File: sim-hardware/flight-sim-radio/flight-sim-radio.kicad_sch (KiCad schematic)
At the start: 0 parts

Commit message: Started on schematic
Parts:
- added U1, U2, U3: LTC-4627JR, Display_7Segment:LTC-4627Jx, symbol Display_Character:LTC-4627JR
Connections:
- new net GND: U1.4 (CAL), U2.4 (CAL), U3.4 (CAL)
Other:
- note added: "Seven Segment Displays"

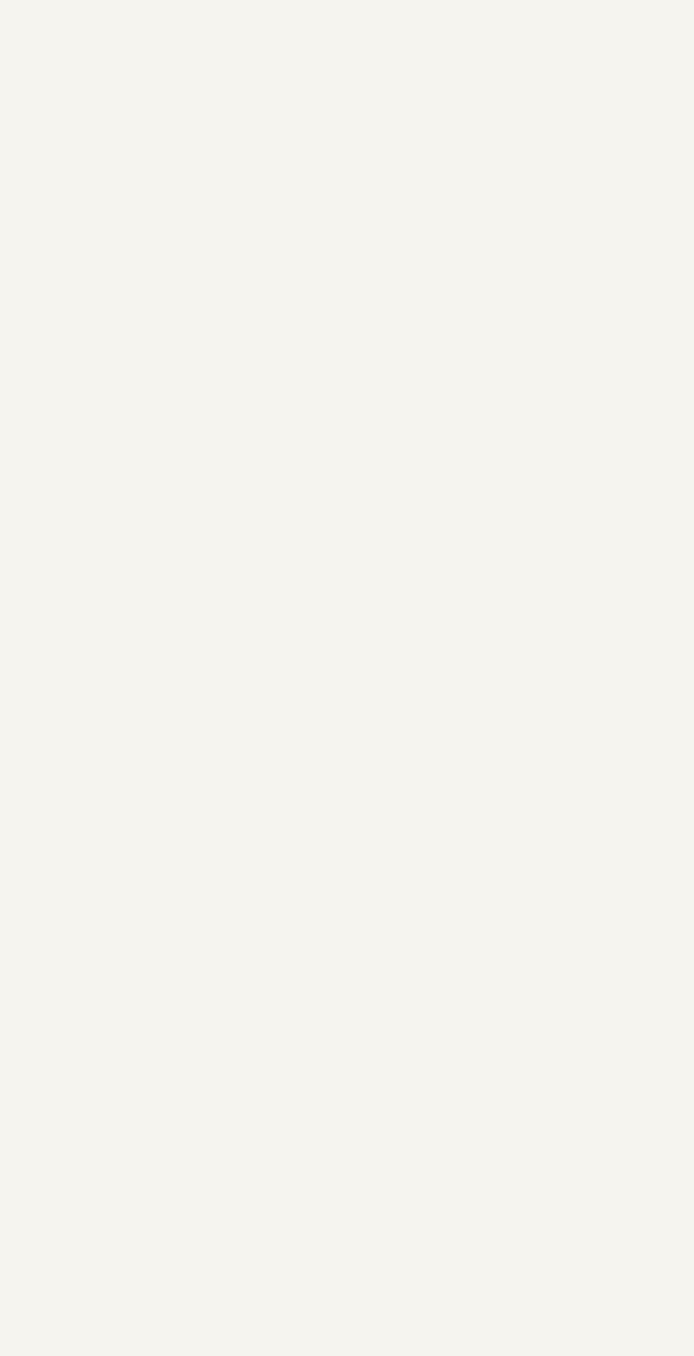
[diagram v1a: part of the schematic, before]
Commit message: LED driver added
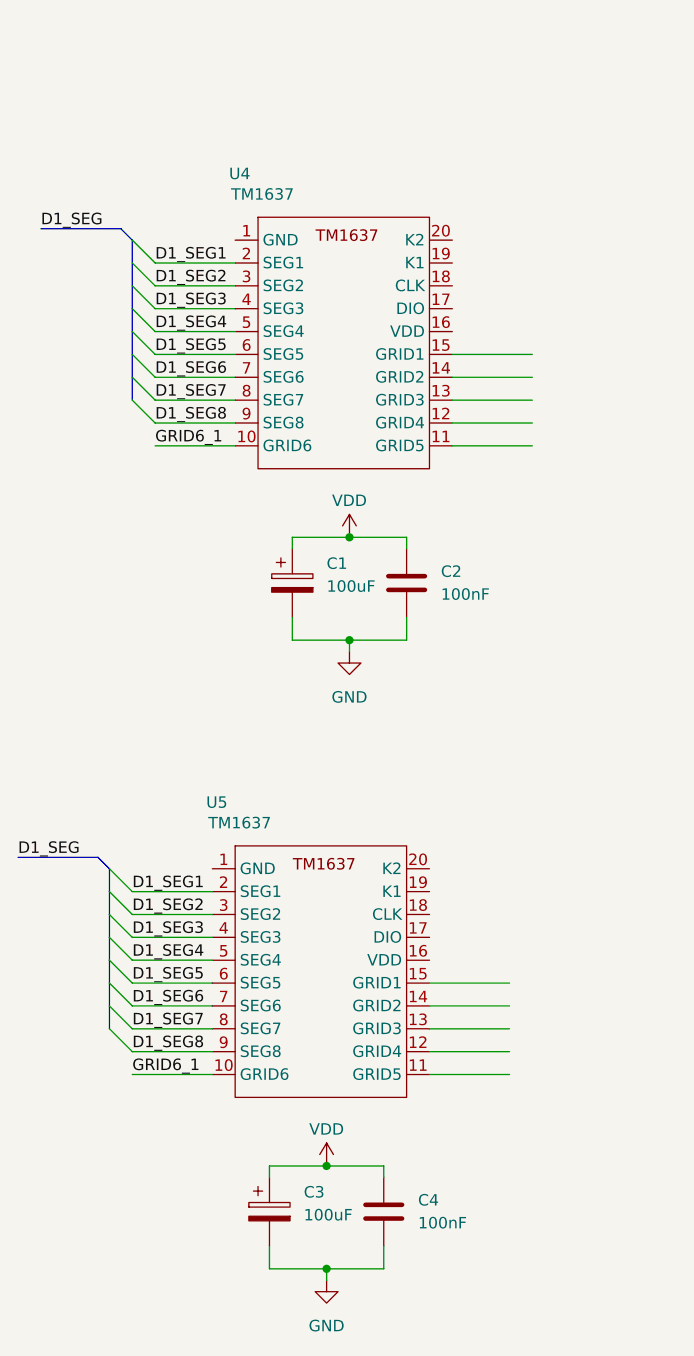
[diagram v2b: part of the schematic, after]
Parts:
- added C1, C3: 100uF, symbol Device:C_Polarized
- added C2, C4: 100nF, symbol Device:C
- added U4, U5: TM1637, Package_DIP:DIP-20_W7.62mm, symbol Radio_Components:TM1637
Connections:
- net GND: now also C1.2, C2.2, C3.2, C4.2
- new net D1_SEG1: U4.2 (SEG1), U5.2 (SEG1)
- new net D1_SEG2: U4.3 (SEG2), U5.3 (SEG2)
- new net D1_SEG3: U4.4 (SEG3), U5.4 (SEG3)
- new net D1_SEG4: U4.5 (SEG4), U5.5 (SEG4)
- new net D1_SEG5: U4.6 (SEG5), U5.6 (SEG5)
- new net D1_SEG6: U4.7 (SEG6), U5.7 (SEG6)
- new net D1_SEG7: U4.8 (SEG7), U5.8 (SEG7)
- new net D1_SEG8: U4.9 (SEG8), U5.9 (SEG8)
- new net GRID6_1: U4.10 (GRID6), U5.10 (GRID6)
- new net VDD: C1.1, C2.1, C3.1, C4.1

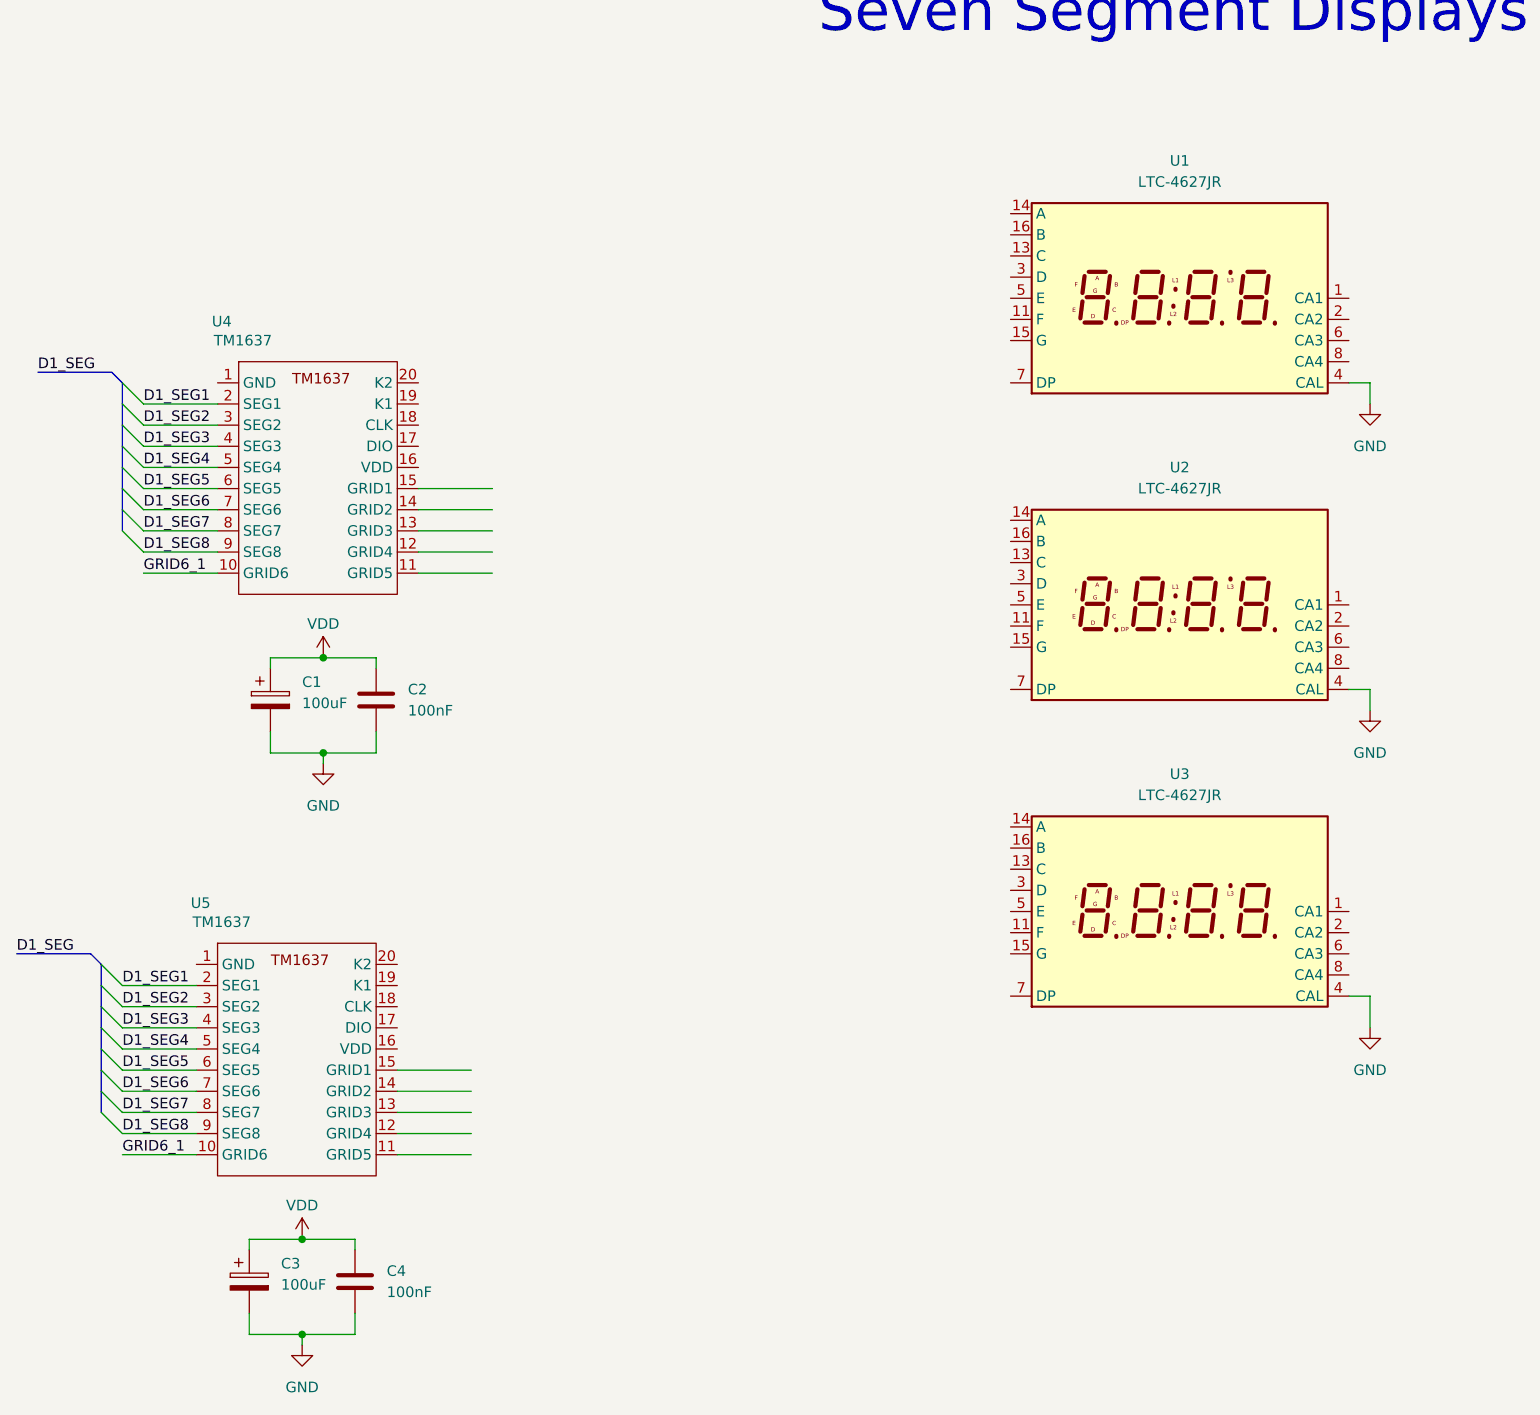
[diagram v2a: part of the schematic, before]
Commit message: LED driver wired
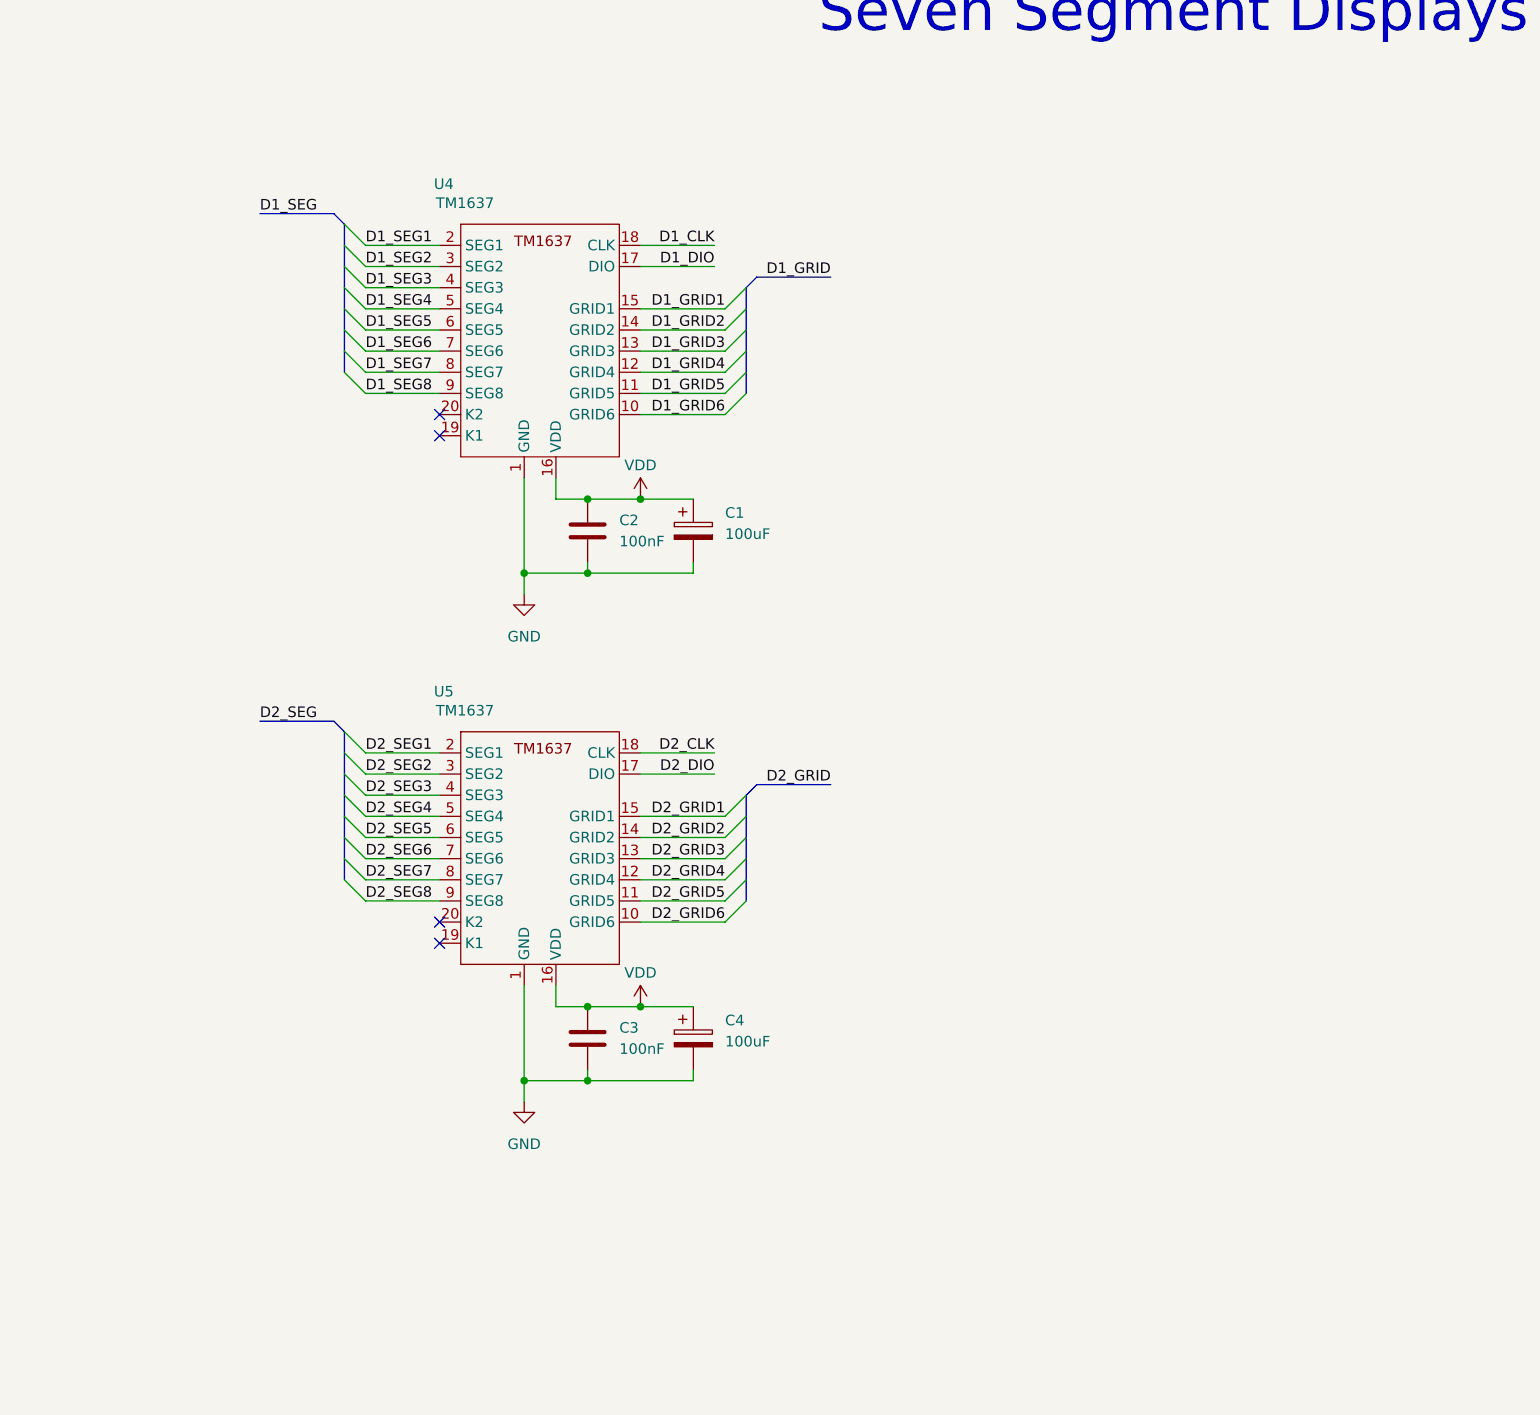
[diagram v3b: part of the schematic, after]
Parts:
- removed C3: 100uF, symbol Device:C_Polarized
- removed C4: 100nF, symbol Device:C
- removed U1, U2, U3: LTC-4627JR, Display_7Segment:LTC-4627Jx, symbol Display_Character:LTC-4627JR
- added C3: 100nF, symbol Device:C
- added C4: 100uF, symbol Device:C_Polarized
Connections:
- net D1_SEG1: no longer U5.2 (SEG1)
- net D1_SEG2: no longer U5.3 (SEG2)
- net D1_SEG3: no longer U5.4 (SEG3)
- net D1_SEG4: no longer U5.5 (SEG4)
- net D1_SEG5: no longer U5.6 (SEG5)
- net D1_SEG6: no longer U5.7 (SEG6)
- net D1_SEG7: no longer U5.8 (SEG7)
- net D1_SEG8: no longer U5.9 (SEG8)
- net GND: now also U4.1 (GND), U5.1 (GND), C3.2, C4.2
- net VDD: now also U4.16 (VDD), U5.16 (VDD), C3.1, C4.1
- net D2_GRID5: now reaches U5.11 (GRID5)
- net D2_GRID4: now reaches U5.12 (GRID4)
- net D2_GRID3: now reaches U5.13 (GRID3)
- net D2_GRID2: now reaches U5.14 (GRID2)
- net D2_GRID1: now reaches U5.15 (GRID1)
- net D2_DIO: now reaches U5.17 (DIO)
- net D2_CLK: now reaches U5.18 (CLK)
- net D1_GRID5: now reaches U4.11 (GRID5)
- net D1_GRID4: now reaches U4.12 (GRID4)
- net D1_GRID3: now reaches U4.13 (GRID3)
- net D1_GRID2: now reaches U4.14 (GRID2)
- net D1_GRID1: now reaches U4.15 (GRID1)
- net D1_DIO: now reaches U4.17 (DIO)
- net D1_CLK: now reaches U4.18 (CLK)
- net GRID6_1 renamed D1_GRID6
- net D1_GRID6: no longer U5.10 (GRID6)
- new net D2_GRID6: U5.10 (GRID6)
- new net D2_SEG1: U5.2 (SEG1)
- new net D2_SEG2: U5.3 (SEG2)
- new net D2_SEG3: U5.4 (SEG3)
- new net D2_SEG4: U5.5 (SEG4)
- new net D2_SEG5: U5.6 (SEG5)
- new net D2_SEG6: U5.7 (SEG6)
- new net D2_SEG7: U5.8 (SEG7)
- new net D2_SEG8: U5.9 (SEG8)
- no-connect marks 0 -> 4
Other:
- moved on the sheet: C1, C2, U4

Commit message: Schematic Draft finished
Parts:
- added C5: 100uF, Capacitor_THT:CP_Axial_L10.0mm_D4.5mm_P15.00mm_Horizontal, symbol Device:C_Polarized
- added C6: 100nF, Capacitor_THT:C_Axial_L3.8mm_D2.6mm_P7.50mm_Horizontal, symbol Device:C
- added D1, D2: FJ3661AH, Package_DIP:DIP-24_W7.62mm, symbol Radio_Components:FJ3661AH
- added J1: Conn_01x04, Connector_PinHeader_2.54mm:PinHeader_1x04_P2.54mm_Vertical, symbol Connector_Generic:Conn_01x04
- added J2: Conn_01x03, Connector_PinHeader_2.54mm:PinHeader_1x03_P2.54mm_Vertical, symbol Connector_Generic:Conn_01x03
- added J3: Conn_01x08, Connector_PinHeader_2.54mm:PinHeader_1x08_P2.54mm_Vertical, symbol Connector_Generic:Conn_01x08
- added R1, R2, R3, R4: 1k, Resistor_THT:R_Axial_DIN0414_L11.9mm_D4.5mm_P15.24mm_Horizontal, symbol Device:R
- added SW1: SW_Push, Button_Switch_THT:SW_PUSH-12mm, symbol Switch:SW_Push
- added SW2: SW_Rotary_1x7_MP, Connector_PinHeader_2.54mm:PinHeader_1x09_P2.54mm_Vertical, symbol Switch:SW_Rotary_1x7_MP
- added SW3, SW4: RotaryEncoder_Switch, Rotary_Encoder:RotaryEncoder_Alps_EC11E-Switch_Vertical_H20mm_CircularMountingHoles, symbol Device:RotaryEncoder_Switch
- added U1: 74LS148, Package_DIP:DIP-16_W7.62mm, symbol 74xx:74LS148
- C1, C2, C4: footprint (none) -> Capacitor_THT:CP_Axial_L10.0mm_D4.5mm_P15.00mm_Horizontal
- C3: footprint (none) -> Capacitor_THT:C_Axial_L3.8mm_D2.6mm_P7.50mm_Horizontal
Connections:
- net D1_CLK: now also J1.1 (Pin_1)
- net D1_DIO: now also J1.2 (Pin_2)
- net D1_GRID1: now also D1.22 (Digit_1)
- net D1_GRID2: now also D1.3 (Digit_2)
- net D1_GRID3: now also D1.4 (Digit_3)
- net D1_GRID4: now also D1.16 (Digit_4)
- net D1_GRID5: now also D1.13 (Digit_5)
- net D1_GRID6: now also D1.12 (Digit_6)
- net D1_SEG1: now also D1.15 (SEG_A)
- net D1_SEG2: now also D1.20 (SEG_B)
- net D1_SEG3: now also D1.19 (SEG_C)
- net D1_SEG4: now also D1.5 (SEG_D)
- net D1_SEG5: now also D1.1 (SEG_E)
- net D1_SEG6: now also D1.14 (SEG_F)
- net D1_SEG7: now also D1.17 (SEG_G)
- net D1_SEG8: now also D1.8 (DP)
- net D2_CLK: now also J1.3 (Pin_3)
- net D2_DIO: now also J1.4 (Pin_4)
- net D2_GRID1: now also D2.22 (Digit_1)
- net D2_GRID2: now also D2.3 (Digit_2)
- net D2_GRID3: now also D2.4 (Digit_3)
- net D2_GRID4: now also D2.16 (Digit_4)
- net D2_GRID5: now also D2.13 (Digit_5)
- net D2_GRID6: now also D2.12 (Digit_6)
- net D2_SEG1: now also D2.15 (SEG_A)
- net D2_SEG2: now also D2.20 (SEG_B)
- net D2_SEG3: now also D2.19 (SEG_C)
- net D2_SEG4: now also D2.5 (SEG_D)
- net D2_SEG5: now also D2.1 (SEG_E)
- net D2_SEG6: now also D2.14 (SEG_F)
- net D2_SEG7: now also D2.17 (SEG_G)
- net D2_SEG8: now also D2.8 (DP)
- net GND: now also C5.2, C6.1, J2.1 (Pin_1), J2.3 (Pin_3), R2.1, R3.1, R4.1, SW1.1, U1.8 (GND)
- net VDD: now also C5.1, C6.2, J2.2 (Pin_2), U1.16 (VCC)
- new net: R3.2, SW3.C
- new net: R2.2, SW2.8
- new net: R4.2, SW4.C
- new net: R1.1, SW1.2
- new net RSWO_1: J3.2 (Pin_2), U1.9 (S0)
- new net RSWO_2: J3.3 (Pin_3), U1.7 (S1)
- new net RSWO_3: J3.4 (Pin_4), U1.6 (S2)
- new net RSW_1: SW2.1, U1.10 (IO)
- new net RSW_2: SW2.2, U1.11 (I1)
- new net RSW_3: SW2.3, U1.12 (I2)
- new net RSW_4: SW2.4, U1.13 (I3)
- new net RSW_5: SW2.5, U1.1 (I4)
- new net RSW_6: SW2.6, U1.2 (I5)
- new net RSW_7: SW2.7, U1.3 (I6)
- new net button_1: J3.1 (Pin_1), R1.2
- new net rotaryEI_A: J3.5 (Pin_5), SW4.A
- new net rotaryEI_B: J3.6 (Pin_6), SW4.B
- new net rotaryEO_A: J3.7 (Pin_7), SW3.A
- new net rotaryEO_B: J3.8 (Pin_8), SW3.B
- no-connect marks 4 -> 13
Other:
- note added: "Power"
- note added: "User Input"
- moved on the sheet: C1, C2, C3, C4, U4, U5

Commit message: 7 Segment Models created
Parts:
- D1, D2: footprint Package_DIP:DIP-24_W7.62mm -> radio_footprints:FJ3661AH-DIP22
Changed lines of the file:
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@@
 	)
 	(symbol
+		(lib_name "FJ3661AH_1")
 		(lib_id "Radio_Components:FJ3661AH")
 		(at 321.31 127 0)
@@
 			)
 		)
-		(property "Footprint" "Package_DIP:DIP-24_W7.62mm"
+		(property "Footprint" "radio_footprints:FJ3661AH-DIP22"
 			(at 321.31 127 0)
 			(effects
@@
 			)
 		)
-		(property "Footprint" "Package_DIP:DIP-24_W7.62mm"
+		(property "Footprint" "radio_footprints:FJ3661AH-DIP22"
 			(at 321.31 66.04 0)
 			(effects
